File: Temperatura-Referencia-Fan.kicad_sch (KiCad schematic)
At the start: 3 parts, among them M1 Fan_3pin, U13 LM35-NEB

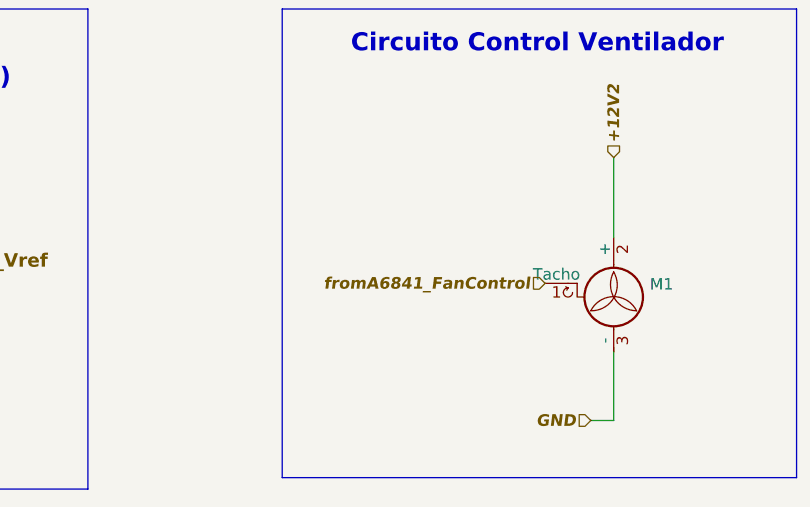
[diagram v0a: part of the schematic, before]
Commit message: Pads mas grandes y correccion de vias
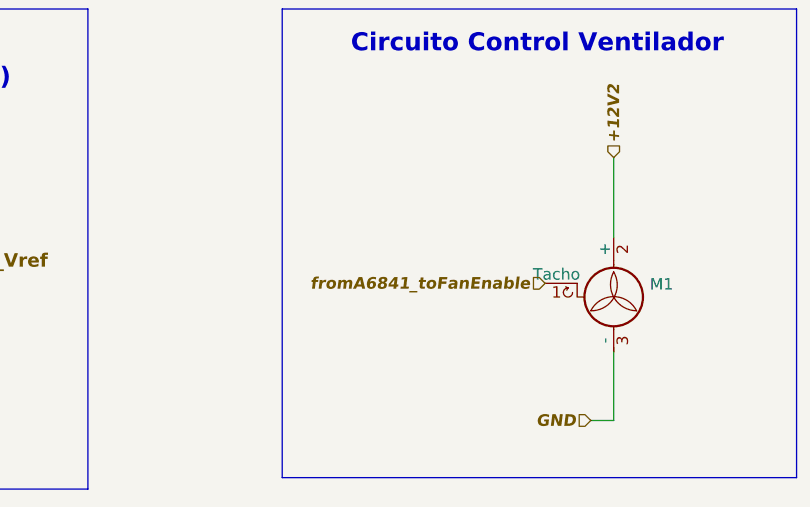
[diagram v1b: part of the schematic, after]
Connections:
- net fromA6841_FanControl renamed fromA6841_toFanEnable
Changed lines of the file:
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@@
     (effects (font (size 1.2954 1.2954) (thickness 0.2591) bold italic) (justify right))
   )
-  (hierarchical_label "fromA6841_FanControl" (shape input) (at 228.981 103.251 180)
+  (hierarchical_label "fromA6841_toFanEnable" (shape input) (at 228.981 103.251 180)
     (effects (font (size 1.2954 1.2954) (thickness 0.2591) bold italic) (justify right))
   )

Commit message: V4 Ltspice
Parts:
- renumbered U13 to U25
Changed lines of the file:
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@@
   (symbol (lib_id "Sensor_Temperature:LM35-NEB") (at 61.341 103.251 0) (unit 1)
     (in_bom yes) (on_board yes)
-    (property "Reference" "U13" (id 0) (at 52.959 102.0826 0)
+    (property "Reference" "U25" (id 0) (at 52.959 102.0826 0)
       (effects (font (size 1.27 1.27)) (justify right))
     )
